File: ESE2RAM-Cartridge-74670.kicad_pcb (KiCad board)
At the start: 2 copper layers, 100 x 60.5 mm, 27 parts, among them IC1 4M SRAM, IC2 4M SRAM, J1 BUS_MSX, J2 8M, U1 74HC670, U2 74HC670, U3 74HC138, U4 74HC00, U5 74HC32

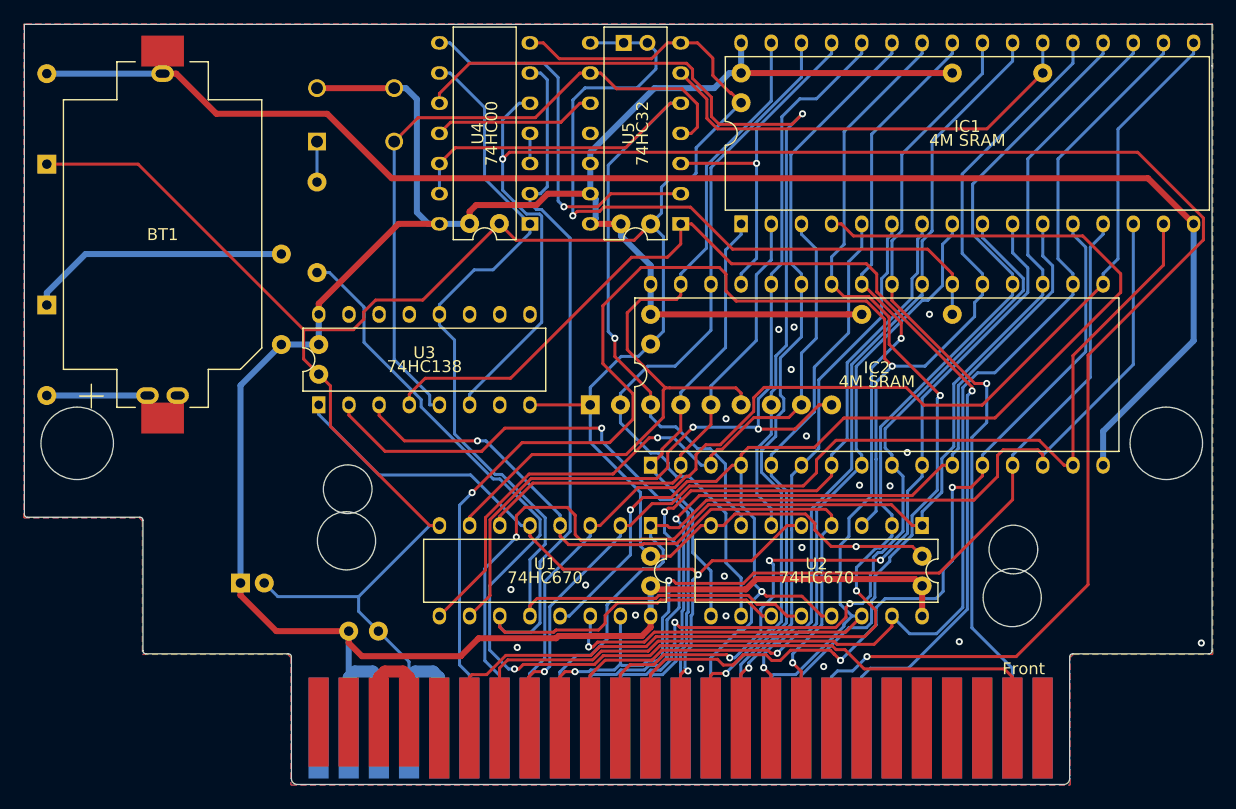
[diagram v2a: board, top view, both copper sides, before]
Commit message: Modified Schematic
部品の配置およびフットプリントの修正と、ガーバーデータへの反映
Modify part placement and footprint and reflect in Gerber data.
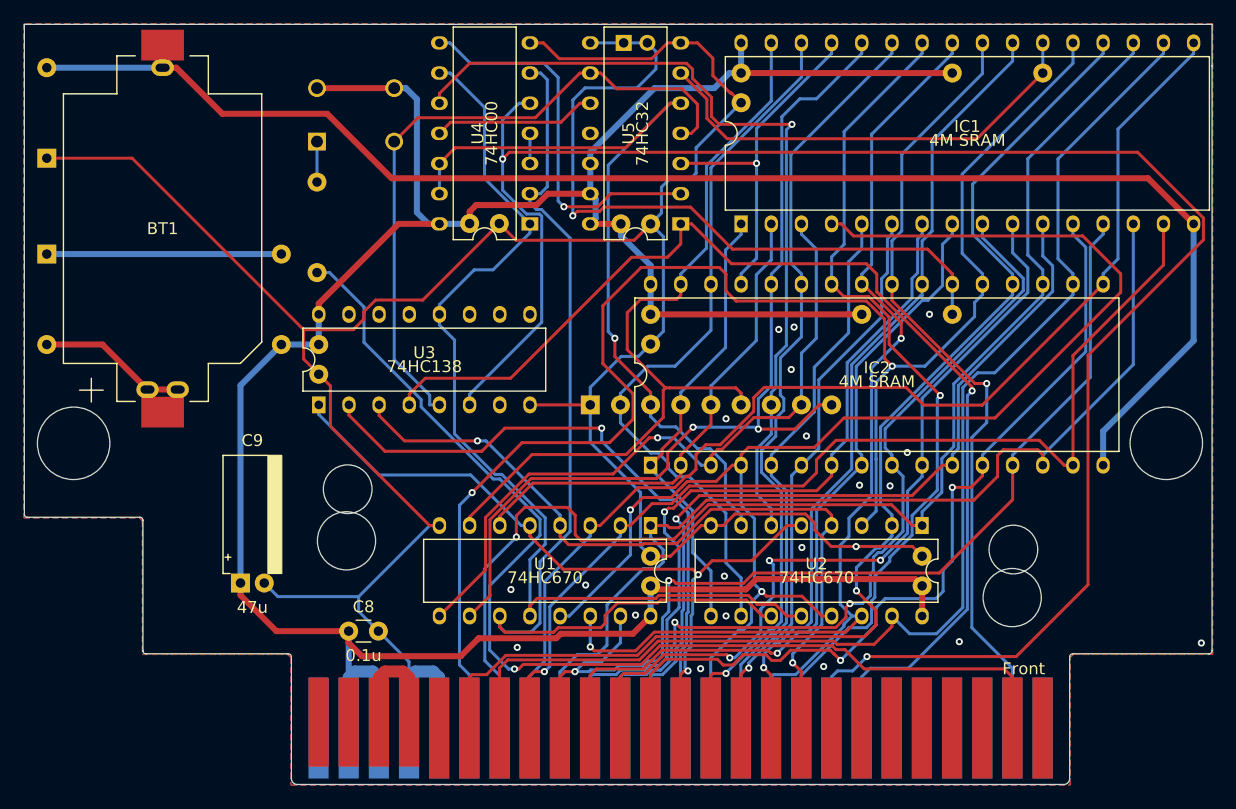
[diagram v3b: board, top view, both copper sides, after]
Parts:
- C8: moved to F.Cu
- C9: footprint Capacitor_THT:CP_Radial_D5.0mm_P2.00mm -> ProjectLibrary:CP_Radial_D5.0mm_P2.00mm_Horizontal; moved to F.Cu
- moved D2 4.29 mm to (41.6, 118.7)
- moved C8 2.50 mm to (67.0, 150.4), turned to 0 degrees
- moved BT1 0.50 mm to (51.4, 116.6)
- moved D1 0.50 mm to (41.6, 110.6)
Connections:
- C8 pad 1: GND -> +5V
- C8 pad 2: +5V -> GND
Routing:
- net Net-(BT1-+): track 9.73 -> 13.8 mm
- net /D0: track 82.7 -> 85.7 mm
- net /EN_WR: track 73.1 -> 70.6 mm
- net Net-(D2-K): track 22.1 -> 19.8 mm
- net /~{RAM0_CE}: track 37.9 -> 38.6 mm
- net +5V: track 235.7 -> 235.2 mm

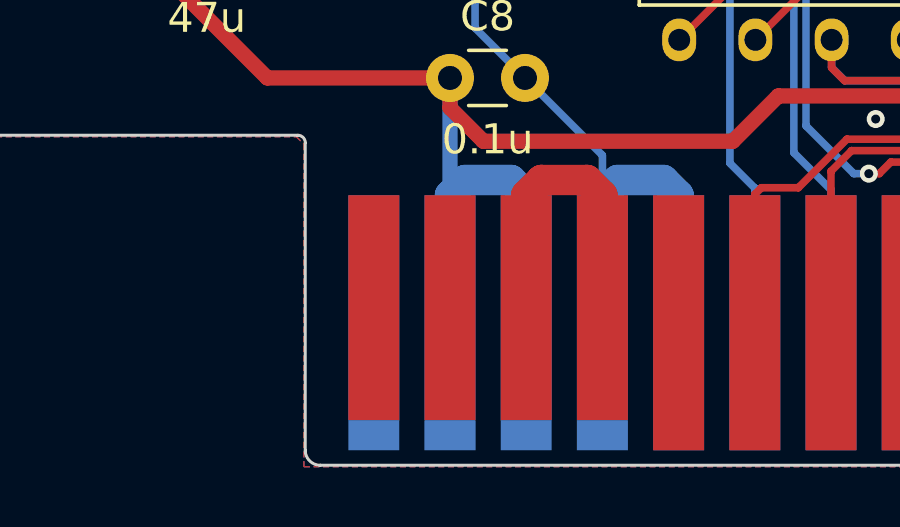
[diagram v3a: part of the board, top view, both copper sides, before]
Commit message: Modified Schematic
カードエッジコネクタのパッド形状(SW2/+12V/-12V)を修正
Corrected the pad shape (SW2/+12V/-12V) of the card edge connector.
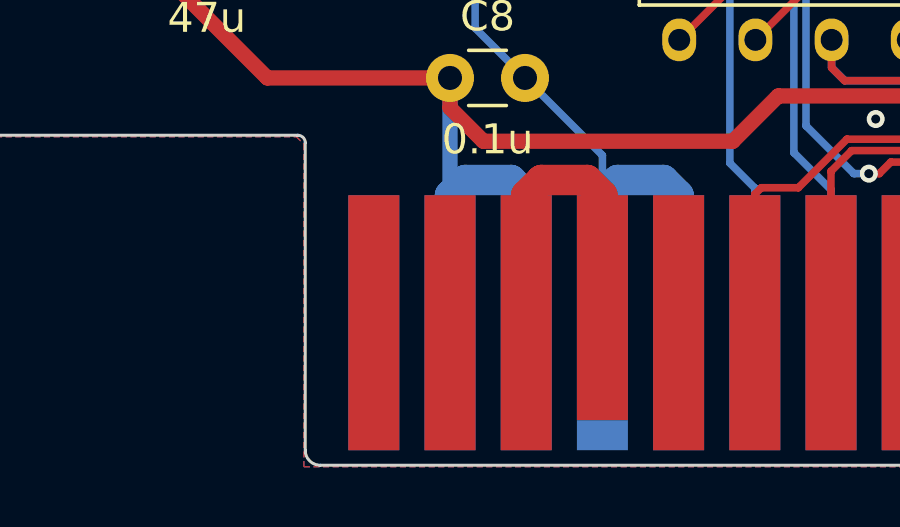
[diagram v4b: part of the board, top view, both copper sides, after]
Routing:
- net Net-(J1-SW1): track 10.5 -> 11.0 mm
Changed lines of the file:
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@@
         (effects (font (size 1 1) (thickness 0.153)) (justify left bottom))
+    )
+    (fp_text user "PCB 10cm square size" (at 0 -95.537 unlocked) (layer "Dwgs.User")
+        (effects (font (size 1 1) (thickness 0.15)) (justify top))
     )
     (fp_text user "Short cartridge size" (at 0 -59.037 unlocked) (layer "Dwgs.User")
         (effects (font (size 1 1) (thickness 0.153)) (justify top))
-    )
-    (fp_text user "PCB 10cm square size" (at 0 -95.537 unlocked) (layer "Dwgs.User")
-        (effects (font (size 1 1) (thickness 0.15)) (justify top))
     )
     (fp_text user "Tall cartridge size" (at 0 -123.037 unlocked) (layer "Dwgs.User")
@@
       (net 22 "/D6") (pinfunction "D6") (pintype "passive"))
     (pad "41" connect rect (at -20.32 -0.44) (size 1.7 8.5) (layers "B.Cu" "B.Mask")
-      (net 2 "GND") (pinfunction "GND") (pintype "passive") (zone_connect 2))
+      (net 2 "GND") (pinfunction "GND") (pintype "passive"))
     (pad "42" connect rect (at -20.32 -0.44) (size 1.7 8.5) (layers "F.Cu" "F.Mask")
       (net 51 "unconnected-(J1-CLOCK-Pad42)") (pinfunction "CLOCK") (pintype "passive+no_connect"))
     (pad "43" connect rect (at -22.86 -0.44) (size 1.7 8.5) (layers "B.Cu" "B.Mask")
-      (net 2 "GND") (pinfunction "GND") (pintype "passive") (zone_connect 2))
+      (net 2 "GND") (pinfunction "GND") (pintype "passive"))
     (pad "44" connect rect (at -22.86 -0.94) (size 1.7 7.5) (layers "F.Cu" "F.Mask")
       (net 52 "Net-(J1-SW1)") (pinfunction "SW1") (pintype "passive"))
     (pad "45" connect rect (at -25.4 -0.44) (size 1.7 8.5) (layers "B.Cu" "B.Mask")
       (net 1 "+5V") (pinfunction "+5V") (pintype "passive"))
-    (pad "46" connect rect (at -25.4 -0.94) (size 1.7 7.5) (layers "F.Cu" "F.Mask")
+    (pad "46" connect rect (at -25.4 -0.44) (size 1.7 8.5) (layers "F.Cu" "F.Mask")
       (net 52 "Net-(J1-SW1)") (pinfunction "SW2") (pintype "passive"))
     (pad "47" connect rect (at -27.94 -0.44) (size 1.7 8.5) (layers "B.Cu" "B.Mask")
       (net 1 "+5V") (pinfunction "+5V") (pintype "passive"))
-    (pad "48" connect rect (at -27.94 -0.94) (size 1.7 7.5) (layers "F.Cu" "F.Mask")
+    (pad "48" connect rect (at -27.94 -0.44) (size 1.7 8.5) (layers "F.Cu" "F.Mask")
       (net 53 "unconnected-(J1-+12V-Pad48)") (pinfunction "+12V") (pintype "passive+no_connect"))
     (pad "49" connect rect (at -30.48 -0.44) (size 1.7 8.5) (layers "B.Cu" "B.Mask")
       (net 54 "unconnected-(J1-SOUND-Pad49)") (pinfunction "SOUND") (pintype "passive+no_connect"))
-    (pad "50" connect rect (at -30.48 -0.94) (size 1.7 7.5) (layers "F.Cu" "F.Mask")
+    (pad "50" connect rect (at -30.48 -0.44) (size 1.7 8.5) (layers "F.Cu" "F.Mask")
       (net 55 "unconnected-(J1--12V-Pad50)") (pinfunction "-12V") (pintype "passive+no_connect"))
     (zone (net 0) (net_name "") (layers "F&B.Cu") (hatch edge 0.5)
@@
   (segment (start 104.42 153.12) (end 104.42 152.370516) (width 0.254) (layer "B.Cu") (net 50))
   (segment (start 106.878 142.382) (end 107.7 141.56) (width 0.254) (layer "B.Cu") (net 50))
+  (segment (start 69.58 154.36) (end 70.088 153.852) (width 1.016) (layer "F.Cu") (net 52))
   (segment (start 71.612 153.852) (end 72.12 154.36) (width 1.016) (layer "F.Cu") (net 52))
-  (segment (start 69.58 154.36) (end 70.088 153.852) (width 1.016) (layer "F.Cu") (net 52))
   (segment (start 70.088 153.852) (end 71.612 153.852) (width 1.016) (layer "F.Cu") (net 52))
-  (segment (start 69.58 158.11) (end 69.58 154.36) (width 1.016) (layer "F.Cu") (net 52))
   (segment (start 72.12 154.36) (end 72.12 158.11) (width 1.016) (layer "F.Cu") (net 52))
+  (segment (start 69.58 158.61) (end 69.58 154.36) (width 1.016) (layer "F.Cu") (net 52))
   (segment (start 70.0995 135.3095) (end 67.06 132.27) (width 0.254) (layer "F.Cu") (net 56))
   (segment (start 67.06 132.27) (end 67.06 131.4) (width 0.254) (layer "F.Cu") (net 56))
